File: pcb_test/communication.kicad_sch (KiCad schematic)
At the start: 18 parts, among them U4 ISOW1044, U5 XISOW1432DFMR

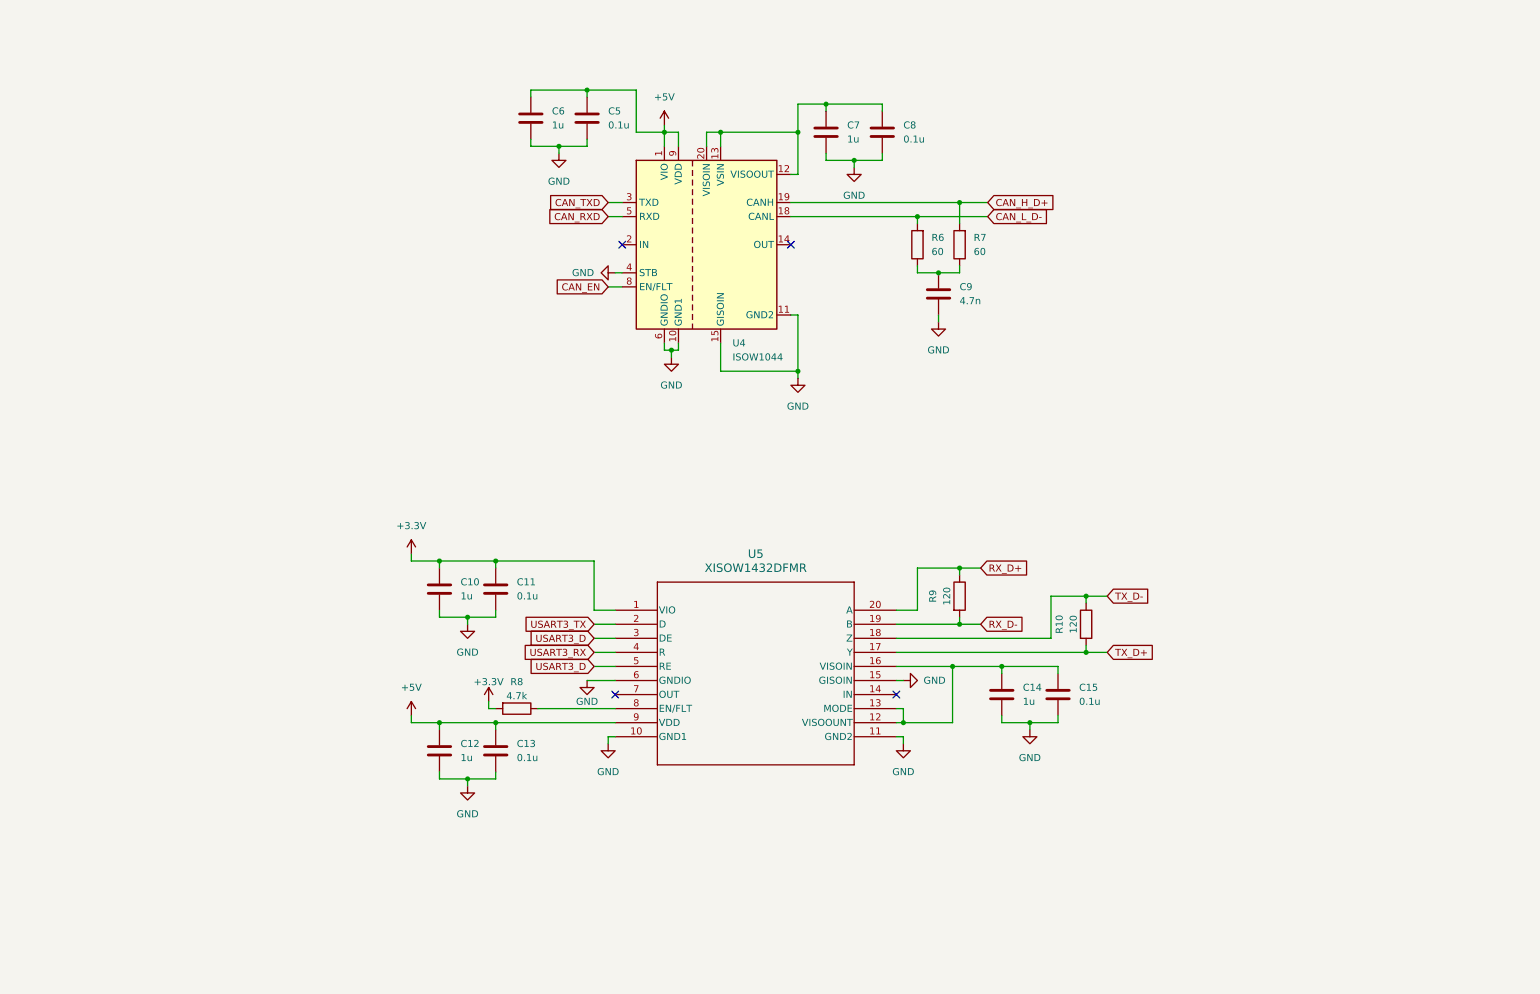
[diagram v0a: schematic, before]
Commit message: Ajout GPS, retrait radio, clean up schemas
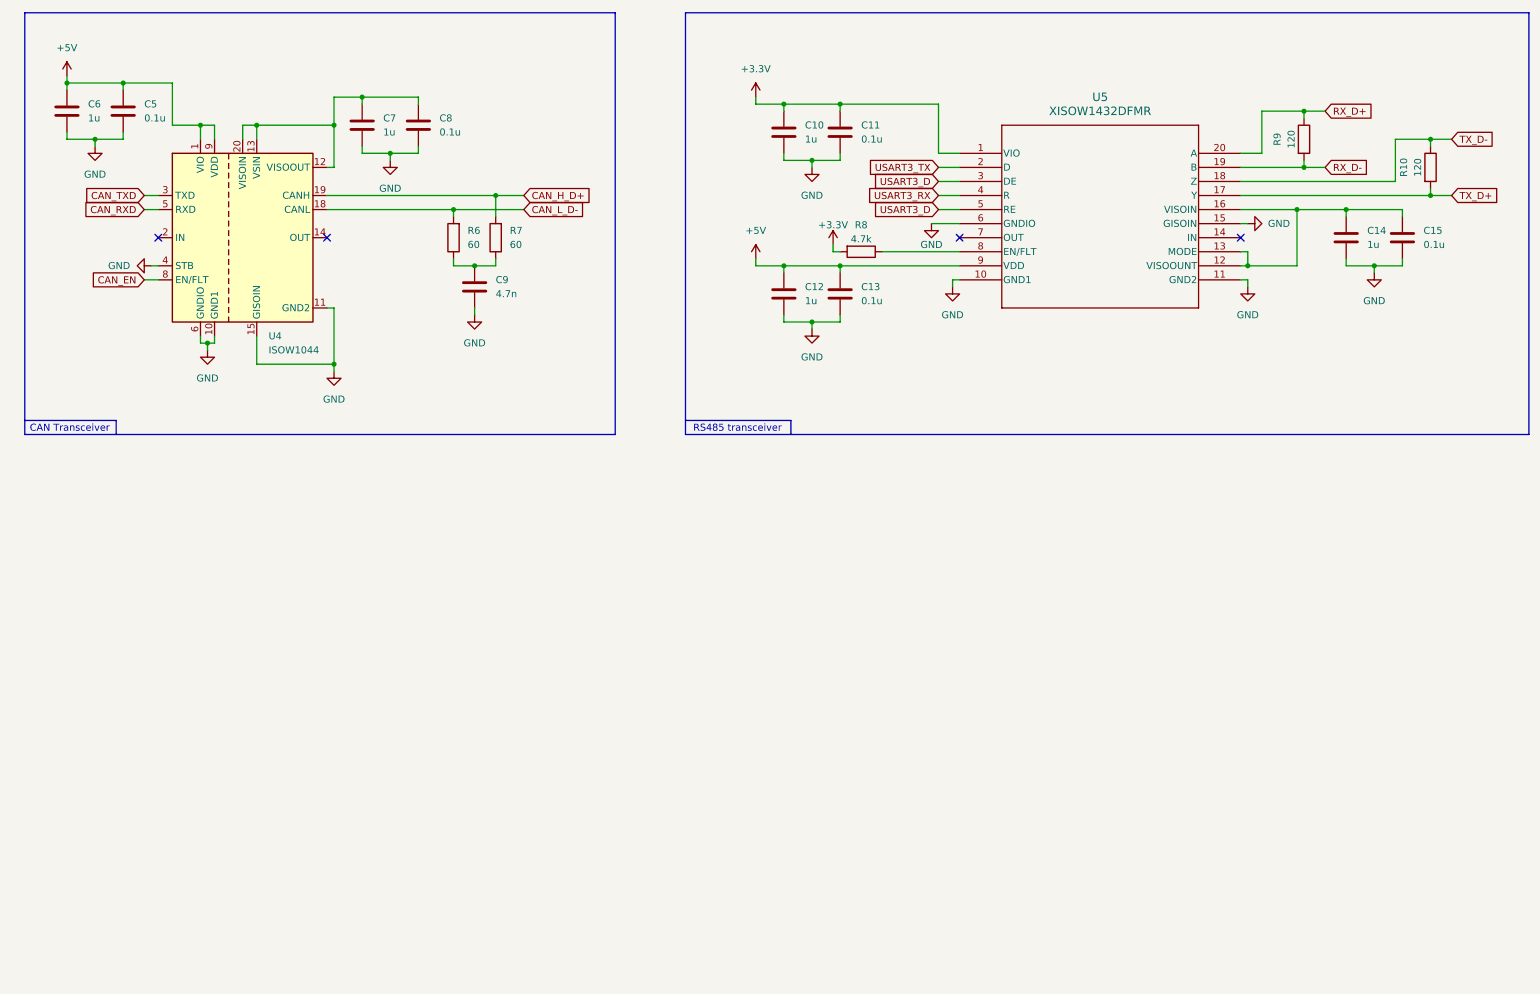
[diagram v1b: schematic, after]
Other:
- note added: "CAN Transceiver"
- note added: "RS485 transceiver"
- moved on the sheet: C10, C11, C12, C13, C14, C15, C5, C6, C7, C8, C9, R10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

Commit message: Ajout testpoints
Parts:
- added TP10, TP11, TP12, TP13, TP14, TP15, TP16, TP17, TP18, TP4, TP5, TP7, TP8, TP9: TestPoint, symbol Connector:TestPoint
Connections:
- net CAN_H_D+: now also TP7.1
- net CAN_L_D-: now also TP8.1
- net CAN_RXD: now also TP5.1
- net CAN_TXD: now also TP4.1
- net GND: now also TP18.1, TP9.1
- net RX_D+: now also TP14.1
- net RX_D-: now also TP15.1
- net TX_D+: now also TP16.1
- net TX_D-: now also TP17.1
- net USART3_D: now also TP12.1; no longer U5.5 (RE)
- net USART3_RX: now also TP11.1
- net USART3_TX: now also TP10.1
- new net USART3_RE: TP13.1, U5.5 (RE)

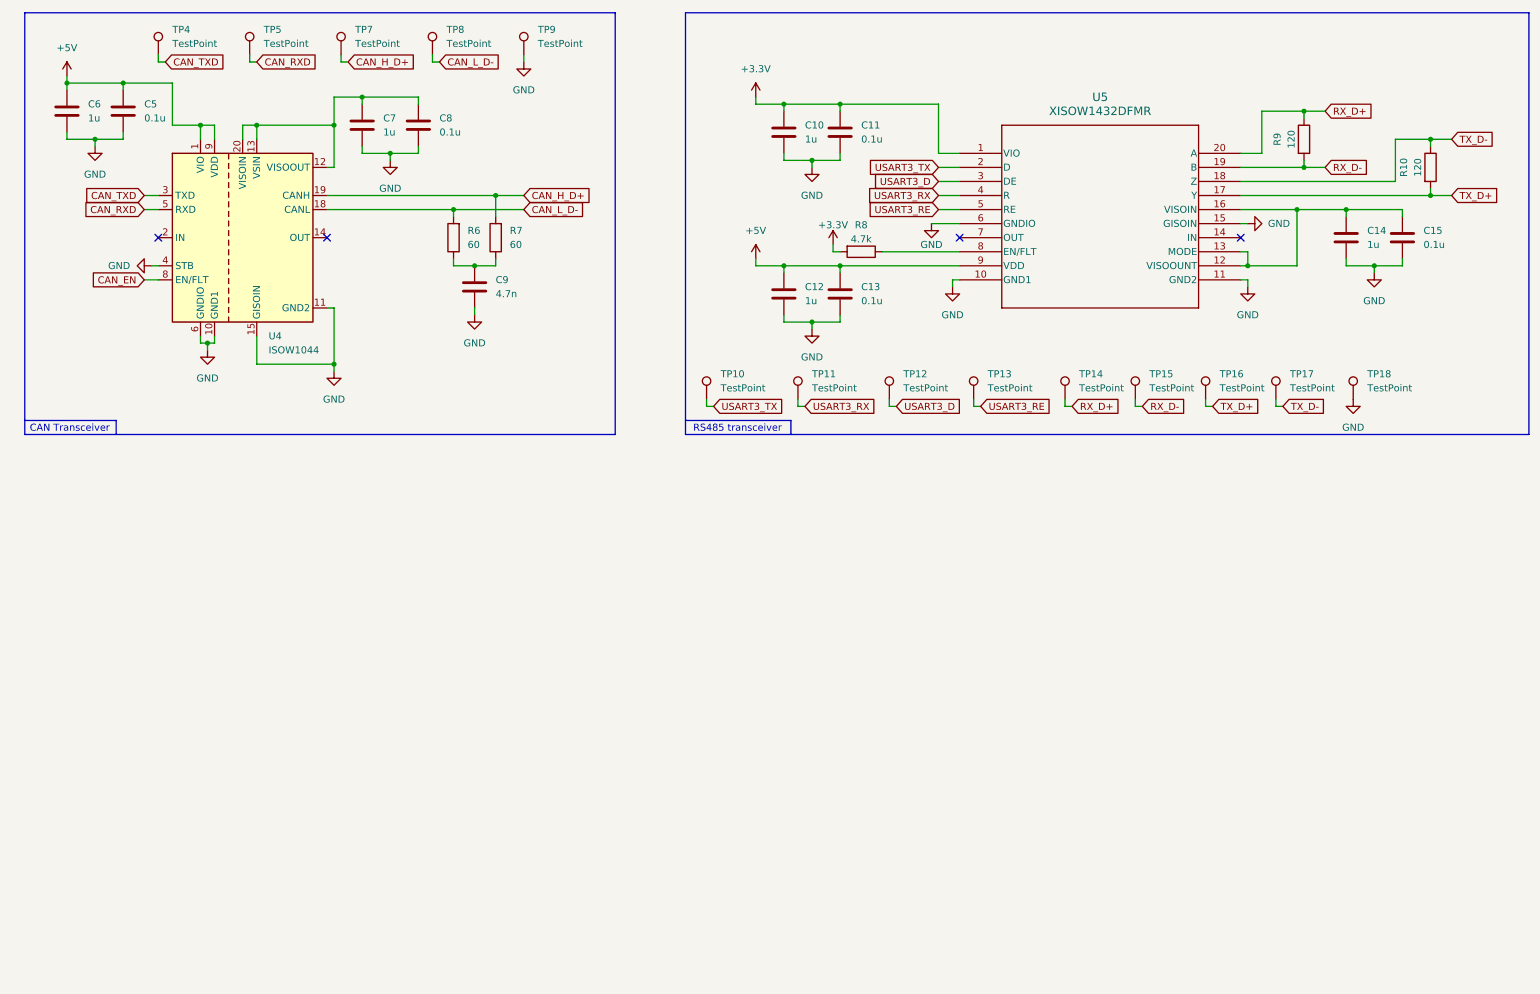
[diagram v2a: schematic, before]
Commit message: refait alimentation, changement MCU, separation schema eMMC/octospi, reajout RF
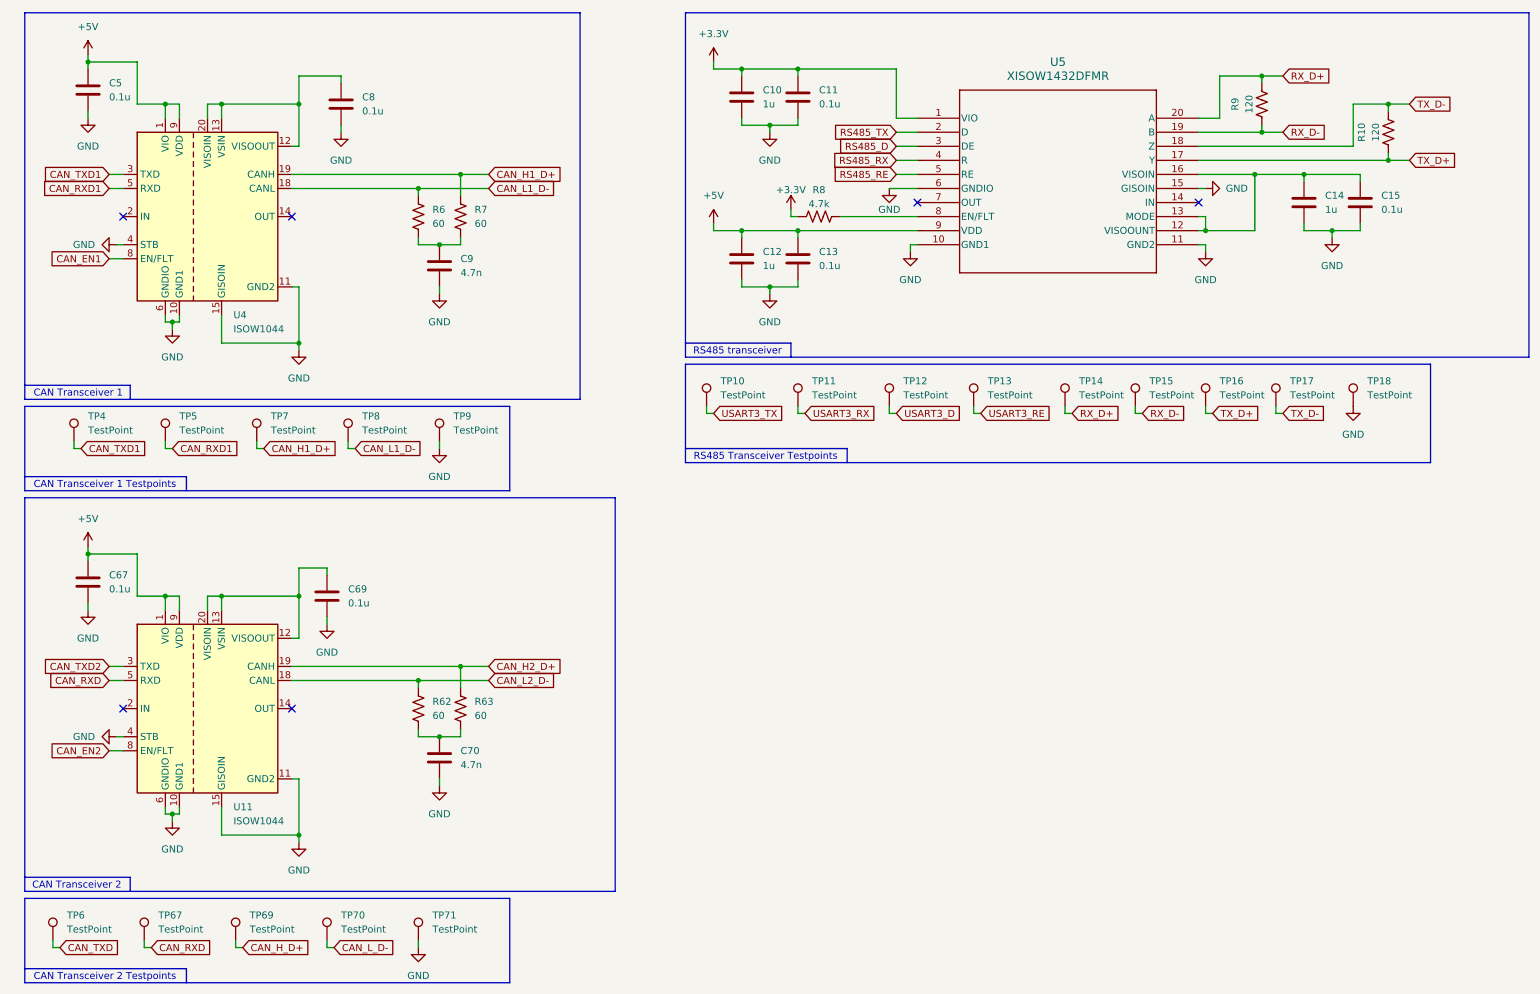
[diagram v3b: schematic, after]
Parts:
- removed C6, C7: 1u, symbol Device:C
- added C67, C69: 0.1u, symbol Device:C
- added C70: 4.7n, symbol Device:C
- added R62, R63: 60, symbol Device:R_US
- added TP6, TP67, TP69, TP70, TP71: TestPoint, symbol Connector:TestPoint
- added U11: ISOW1044, Package_SO:SOIC-20W_7.5x12.8mm_P1.27mm, symbol Interface_CAN_LIN:ISOW1044
- R10, R6, R7, R8, R9: symbol Device:R -> Device:R_US
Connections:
- net +5V: now also C67.1, U11.1 (VIO), U11.9 (VDD)
- net CAN_H_D+: now also TP69.1; no longer R7.2, TP7.1, U4.19 (CANH)
- net CAN_L_D-: now also TP70.1; no longer R6.2, TP8.1, U4.18 (CANL)
- net CAN_RXD: now also TP67.1, U11.5 (RXD); no longer TP5.1, U4.5 (RXD)
- net CAN_TXD: now also TP6.1; no longer TP4.1, U4.3 (TXD)
- net GND: now also C67.2, C69.2, C70.2, TP71.1, U11.10 (GND1), U11.11 (GND2), U11.15 (GISOIN), U11.16 (GISOIN), U11.17 (GISOIN), U11.4 (STB), U11.6 (GNDIO)
- net USART3_D: no longer U5.3 (DE)
- net USART3_RE: no longer U5.5 (RE)
- net USART3_RX: no longer U5.4 (R)
- net USART3_TX: no longer U5.2 (D)
- net CAN_EN renamed CAN_EN1
- new net: C70.1, R62.1, R63.1
- new net: C69.1, U11.12 (VISOOUT), U11.13 (VSIN), U11.20 (VISOIN)
- new net CAN_EN2: U11.8 (EN/FLT)
- new net CAN_H1_D+: R7.2, TP7.1, U4.19 (CANH)
- new net CAN_H2_D+: R63.2, U11.19 (CANH)
- new net CAN_L1_D-: R6.2, TP8.1, U4.18 (CANL)
- new net CAN_L2_D-: R62.2, U11.18 (CANL)
- new net CAN_RXD1: TP5.1, U4.5 (RXD)
- new net CAN_TXD1: TP4.1, U4.3 (TXD)
- new net CAN_TXD2: U11.3 (TXD)
- new net RS485_D: U5.3 (DE)
- new net RS485_RE: U5.5 (RE)
- new net RS485_RX: U5.4 (R)
- new net RS485_TX: U5.2 (D)
- no-connect marks 4 -> 6
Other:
- note added: "CAN Transceiver 1"
- note added: "CAN Transceiver 1 Testpoints"
- note added: "CAN Transceiver 2"
- note added: "CAN Transceiver 2 Testpoints"
- note added: "RS485 Transceiver Testpoints"
- note removed: "CAN Transceiver"
- moved on the sheet: C10, C11, C12, C13, C14, C15, C5, C8, C9, TP10, TP11, TP12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

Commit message: alimentation finale. Retouches testpoints et condo decouplage, finalisation requis, ajout sheet finale.
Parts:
- removed C10, C12: 1u, symbol Device:C
- C70, C9: now not fitted
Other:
- moved on the sheet: C11, C13, C14, C15, C67, C69, R10, R62, R63, R8, R9, TP10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
